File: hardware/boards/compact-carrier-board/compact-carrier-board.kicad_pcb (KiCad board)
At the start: 2 copper layers, 26 x 44 mm, 7 parts

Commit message: fix(pcb): widen 5V net to spec, reposition board, fix stale metadata
5V net was mostly routed at KiCad's 0.6mm default instead of the board's
own documented IPC-2221 target (2A, 1oz copper, 10C rise -> ~0.78mm min).
Widened to 1.0mm for 74.9mm of its 83.9mm total length. The remaining
9mm stays at 0.6mm in two short, unavoidable pinch points (4mm, 5mm)
where the trace passes within 1.27-1.34mm of unrelated J_ESP2 pads and
can't widen without violating clearance. Both pinch points sit downstream
of the branch point that already routes the highest-current load
(J_SERVO) on its own independent, unpinched trace, so worst-case current
through either pinch is bounded by the ESP32 module + J_I2S amp combined
(~1.0-1.1A by datasheet figures, against the pinch's own ~1.65A/10C
capacity) -- real margin, not a bare pass. Verified against Espressif's
ESP32-C3 datasheet (350mA peak WiFi TX) and Analog Devices' MAX98357A
datasheet (3.2W/4ohm rated output, ~700mA computed supply draw at 92%
efficiency).

Widening the traces required refilling the GND copper pour, which
surfaced a real bug: the zone's saved fill went stale relative to the
new geometry, leaving it ~0.0005-0.0015mm from the widened traces --
effectively fused copper, invisible to `kicad-cli pcb drc --refill-zones`
since that flag only recomputes the fill in-memory for the check and
never persists it to the file. A naive Gerber export would have carried
the stale, shorted fill straight into a fab package. Fixed by using
KiCad's own Python API (pcbnew.ZONE_FILLER + pcbnew.SaveBoard) to force
a real refill and re-save; re-verified with `kicad-cli pcb drc` run
*without* --refill-zones specifically to confirm the fix persisted to
disk rather than just passing the same in-memory check again.

Also: repositioned the whole board off the KiCad page origin (was
overlapping the A4 sheet's own border/reference-grid decoration --
cosmetic, no fab effect, verified as an exact rigid translation of every
object); stripped a stale `c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
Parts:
- J_ESP1: footprint carrier:J_ESP1 -> J_ESP1
- J_ESP2: footprint carrier:J_ESP2 -> J_ESP2
- J_I2C_OLED: footprint carrier:J_I2C_OLED -> J_I2C_OLED
- J_I2C_PCA: footprint carrier:J_I2C_PCA -> J_I2C_PCA
- J_I2S: footprint carrier:J_I2S -> J_I2S
- J_PWR: footprint carrier:J_PWR -> J_PWR
- J_SERVO: footprint carrier:J_SERVO -> J_SERVO
- moved J_ESP1 17.7 mm to (25.5, 14.2)
- moved J_ESP2 17.7 mm to (25.5, 29.4)
- moved J_I2C_OLED 17.7 mm to (20.4, 36.5)
- moved J_I2C_PCA 17.7 mm to (20.4, 42.5)
- moved J_I2S 17.7 mm to (31.9, 36.5)
- moved J_PWR 17.7 mm to (21.7, 49.5)
- moved J_SERVO 17.7 mm to (29.3, 49.5)
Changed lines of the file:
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@@
 		)
 	)
-	(footprint "carrier:J_ESP1"
-		(layer "F.Cu")
-		(at 13 1.65)
+	(footprint "J_ESP1"
+		(layer "F.Cu")
+		(at 25.5 14.15)
 		(property "Reference" "J_ESP1"
-			(at -10.466666 -1 0)
+			(at -7.62 2.2 0)
 			(layer "F.SilkS")
 			(effects
@@
 		(embedded_fonts no)
 	)
-	(footprint "carrier:J_I2C_PCA"
-		(layer "F.Cu")
-		(at 7.92 30)
+	(footprint "J_I2C_PCA"
+		(layer "F.Cu")
+		(at 20.42 42.5)
 		(property "Reference" "J_I2C_PCA"
 			(at -4.491429 -2 0)
@@
 		(embedded_fonts no)
 	)
-	(footprint "carrier:J_I2C_OLED"
-		(layer "F.Cu")
-		(at 7.92 24)
+	(footprint "J_I2C_OLED"
+		(layer "F.Cu")
+		(at 20.42 36.5)
 		(property "Reference" "J_I2C_OLED"
 			(at -4.129524 -2 0)
@@
 		(embedded_fonts no)
 	)
-	(footprint "carrier:J_PWR"
-		(layer "F.Cu")
-		(at 9.19 37)
+	(footprint "J_PWR"
+		(layer "F.Cu")
+		(at 21.69 49.5)
 		(property "Reference" "J_PWR"
 			(at -5.01 -2 0)
@@
 		(embedded_fonts no)
 	)
-	(footprint "carrier:J_I2S"
-		(layer "F.Cu")
-		(at 19.35 24)
+	(footprint "J_I2S"
+		(layer "F.Cu")
+		(at 31.85 36.5)
 		(property "Reference" "J_I2S"
 			(at -6.28 -2 0)
@@
 		(embedded_fonts no)
 	)
-	(footprint "carrier:J_ESP2"
-		(layer "F.Cu")
-		(at 13 16.89)
+	(footprint "J_ESP2"
+		(layer "F.Cu")
+		(at 25.5 29.39)
 		(property "Reference" "J_ESP2"
 			(at -10.466666 2.2 0)
@@
 		(embedded_fonts no)
 	)
-	(footprint "carrier:J_SERVO"
-		(layer "F.Cu")
-		(at 16.81 37)
+	(footprint "J_SERVO"
+		(layer "F.Cu")
+		(at 29.31 49.5)
 		(property "Reference" "J_SERVO"
 			(at -2.47 -2 0)
@@
 	)
 	(gr_rect
-		(start 0 0)
-		(end 26 44)
+		(start 12.5 12.5)
+		(end 38.5 56.5)
 		(stroke
 			(width 0.1)
@@
 	)
 	(segment
-		(start 13 37)
-		(end 15.54 37)
-		(width 1)
-		(layer "F.Cu")
-		(net "5V")
-	)
-	(segment
-		(start 2.84 1.65)
-		(end 1.5 10)
+		(start 25.5 49.5)
+		(end 28.04 49.5)
+		(width 1)
+		(layer "F.Cu")
+		(net "5V")
+	)
+	(segment
+		(start 26.77 31.5)
+		(end 26.77 36.5)
+		(width 1)
+		(layer "B.Cu")
+		(net "5V")
+	)
+	(segment
+		(start 15.34 14.15)
+		(end 14 22.5)
+		(width 1)
+		(layer "B.Cu")
+		(net "5V")
+	)
+	(segment
+		(start 14 27)
+		(end 14 32)
 		(width 0.6)
 		(layer "B.Cu")
@@
 	)
 	(segment
-		(start 1 12)
-		(end 14.27 14)
+		(start 13.5 24.5)
+		(end 26.77 26.5)
+		(width 1)
+		(layer "B.Cu")
+		(net "5V")
+	)
+	(segment
+		(start 26.77 26.5)
+		(end 26.77 27.5)
+		(width 1)
+		(layer "B.Cu")
+		(net "5V")
+	)
+	(segment
+		(start 13.5 16.5)
+		(end 13.5 24.5)
+		(width 1)
+		(layer "B.Cu")
+		(net "5V")
+	)
+	(segment
+		(start 15.34 14.15)
+		(end 13.5 16.5)
+		(width 1)
+		(layer "B.Cu")
+		(net "5V")
+	)
+	(segment
+		(start 14 46.5)
+		(end 25.5 46.5)
+		(width 1)
+		(layer "B.Cu")
+		(net "5V")
+	)
+	(segment
+		(start 14 22.5)
+		(end 14 27)
+		(width 1)
+		(layer "B.Cu")
+		(net "5V")
+	)
+	(segment
+		(start 14 32)
+		(end 14 46.5)
+		(width 1)
+		(layer "B.Cu")
+		(net "5V")
+	)
+	(segment
+		(start 26.77 27.5)
+		(end 26.77 31.5)
 		(width 0.6)
 		(layer "B.Cu")
@@
 	)
 	(segment
-		(start 14.27 14)
-		(end 14.27 24)
-		(width 0.6)
-		(layer "B.Cu")
-		(net "5V")
-	)
-	(segment
-		(start 1 4)
-		(end 1 12)
-		(width 0.6)
-		(layer "B.Cu")
-		(net "5V")
-	)
-	(segment
-		(start 2.84 1.65)
-		(end 1 4)
-		(width 0.6)
-		(layer "B.Cu")
-		(net "5V")
-	)
-	(segment
-		(start 1.5 34)
-		(end 13 34)
-		(width 0.6)
-		(layer "B.Cu")
-		(net "5V")
-	)
-	(segment
-		(start 1.5 10)
-		(end 1.5 34)
-		(width 0.6)
-		(layer "B.Cu")
-		(net "5V")
-	)
-	(segment
-		(start 13 34)
-		(end 13 37)
-		(width 0.6)
-		(layer "B.Cu")
-		(net "5V")
-	)
-	(segment
-		(start 11.73 24)
-		(end 11.73 30)
+		(start 25.5 46.5)
+		(end 25.5 49.5)
+		(width 1)
+		(layer "B.Cu")
+		(net "5V")
+	)
+	(segment
+		(start 24.23 36.5)
+		(end 24.23 42.5)
 		(width 0.3)
 		(layer "F.Cu")
@@
 	)
 	(segment
-		(start 4.11 24)
-		(end 4.11 30)
+		(start 16.61 36.5)
+		(end 16.61 42.5)
 		(width 0.25)
 		(layer "F.Cu")
@@
 	)
 	(segment
-		(start 7.92 1.65)
-		(end 4.11 16.89)
+		(start 20.42 14.15)
+		(end 16.61 29.39)
 		(width 0.3)
 		(layer "F.Cu")
@@
 	)
 	(segment
-		(start 4.11 16.89)
-		(end 4.11 24)
+		(start 16.61 29.39)
+		(end 16.61 36.5)
 		(width 0.3)
 		(layer "F.Cu")
@@
 	)
 	(segment
-		(start 10.46 1.65)
-		(end 6.65 16.89)
+		(start 22.96 14.15)
+		(end 19.15 29.39)
 		(width 0.25)
 		(layer "F.Cu")
@@
 	)
 	(segment
-		(start 6.65 24)
-		(end 6.65 30)
+		(start 19.15 36.5)
+		(end 19.15 42.5)
 		(width 0.25)
 		(layer "F.Cu")
@@
 	)
 	(segment
-		(start 6.65 16.89)
-		(end 6.65 24)
+		(start 19.15 29.39)
+		(end 19.15 36.5)
 		(width 0.25)
 		(layer "F.Cu")
@@
 	)
 	(segment
-		(start 9.19 24)
-		(end 9.19 30)
+		(start 21.69 36.5)
+		(end 21.69 42.5)
 		(width 0.25)
 		(layer "F.Cu")
@@
 	)
 	(segment
-		(start 13 1.65)
-		(end 9.19 16.89)
+		(start 25.5 14.15)
+		(end 21.69 29.39)
 		(width 0.25)
 		(layer "F.Cu")
@@
 	)
 	(segment
-		(start 9.19 16.89)
-		(end 9.19 24)
+		(start 21.69 29.39)
+		(end 21.69 36.5)
 		(width 0.25)
 		(layer "F.Cu")
@@
 	)
 	(segment
-		(start 15.54 1.65)
-		(end 16.81 16.89)
+		(start 28.04 14.15)
+		(end 29.31 29.39)
 		(width 0.25)
 		(layer "B.Cu")
@@
 	)
 	(segment
-		(start 16.81 16.89)
-		(end 16.81 24)
+		(start 29.31 29.39)
+		(end 29.31 36.5)
 		(width 0.25)
 		(layer "B.Cu")
@@
 	)
 	(segment
-		(start 18.08 1.65)
-		(end 19.35 16.89)
+		(start 30.58 14.15)
+		(end 31.85 29.39)
 		(width 0.25)
 		(layer "B.Cu")
@@
 	)
 	(segment
-		(start 19.35 16.89)
-		(end 19.35 24)
+		(start 31.85 29.39)
+		(end 31.85 36.5)
 		(width 0.25)
 		(layer "B.Cu")
@@
 	)
 	(segment
-		(start 21.89 16.89)
-		(end 21.89 24)
+		(start 34.39 29.39)
+		(end 34.39 36.5)
 		(width 0.25)
 		(layer "B.Cu")
@@
 	)
 	(segment
-		(start 20.62 1.65)
-		(end 21.89 16.89)
+		(start 33.12 14.15)
+		(end 34.39 29.39)
 		(width 0.25)
 		(layer "B.Cu")
@@
 	)
 	(segment
-		(start 7.92 16.89)
-		(end 7.92 37)
+		(start 20.42 29.39)
+		(end 20.42 49.5)
 		(width 0.3)
 		(layer "F.Cu")
@@
 	)
 	(segment
-		(start 10.46 16.89)
-		(end 10.46 37)
+		(start 22.96 29.39)
+		(end 22.96 49.5)
 		(width 0.3)
 		(layer "F.Cu")
@@
 		(polygon
 			(pts
-				(xy 0.5 0.5) (xy 25.5 0.5) (xy 25.5 43.5) (xy 0.5 43.5)
-			)
-		)
+				(xy 13 13) (xy 38 13) (xy 38 56) (xy 13 56)
+			)
+		)

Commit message: carrier-board: fix mirrored ESP socket, add pin-name silkscreen
The two 1x9 socket rows carried each other's nets: the pad map was the
C3-Zero seen from its PIN side, which is only correct for a socket on the
opposite face. As drawn, a component-side-up module could not mate — 5V
would have landed on GP5.

Caught by handedness, which no rotation can change: on the module
(component side, USB-C up) pins 1-9 run down the left column and 10-18 up
the right, so 1->18 is counter-clockwise; on the old artwork J_ESP1 1->9 ran
left-to-right along the outer row and J_ESP2 10->18 right-to-left along the
inner row, i.e. clockwise.

Swap the two footprints' Y positions (14.15 <-> 29.39) so the nets land on
the correct rows, and re-route. Nothing mechanical moves: the exported
PTH.drl and Edge_Cuts.gm1 are byte-identical to the previous revision, all
37 holes stay at 0.9mm, and the five wire-end connectors do not move. The
module's USB-C still overhangs the 5V-bus edge.

Re-route side effects, all measured:
- 5V: 83.901mm with 9mm at 0.600mm -> 44.939mm entirely at 1.000mm, so the
  net now meets its own IPC-2221 target everywhere; an acute-angle acid
  trap at the old 5V pad is gone.
- 3V3/SDA/SCL moved to B.Cu (all pads are THT, so no vias), which frees
  F.Cu for D+/D- to pass the row they now cross.
- D+/D-: 20.110 -> 36.088mm each, exactly length-matched, one 1.27mm jog
  per line at 0.420mm to the nearest pad edge (was 0.270mm worst case).
- GND pour +6.9%, one island, all six GND pads on 4 thermal spokes.

Add the silkscreen that would have made this visible: 18 socket pin names
and a USB-end arrow at 1.0mm/0.15mm, JLCPCB's standard-font minimum. The
board previously carried nothing but seven reference designators. Placement
was verified geometrically, not by DRC — this project sets
min_silk_clearance to 0, so DRC would not flag an overlap.

kicad-cli pcb drc --severity-all, run without --refill-zones: 0 violations,
0 unconnected items. The on-disk zone fill is vertex-exa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
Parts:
- moved J_ESP1 15.2 mm to (25.5, 29.4)
- moved J_ESP2 15.2 mm to (25.5, 14.2)
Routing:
- net 5V: track 83.9 -> 44.9 mm
- net USB_DP: track 20.1 -> 36.1 mm
- net USB_DM: track 20.1 -> 36.1 mm
- net BCLK: track 22.4 -> 7.33 mm
- net LRCLK: track 22.4 -> 7.33 mm
- net DIN: track 22.4 -> 7.33 mm
- net SCL: track 28.8 -> 14.7 mm
- net SDA: track 28.8 -> 14.7 mm
- net 3V3: track 28.8 -> 14.7 mm
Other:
- board text added: "3V3"
- board text added: "5V"
- board text added: "GND"
- board text added: "GP0"
- board text added: "GP1"
- board text added: "GP10"
- board text added: "GP18"
- board text added: "GP19"
- board text added: "GP2"
- board text added: "GP20"
- board text added: "GP21"
- board text added: "GP3"
- board text added: "GP4"
- board text added: "GP5"
- board text added: "GP6"
- board text added: "GP7"
- board text added: "GP8"
- board text added: "GP9"
- board text added: "USB"

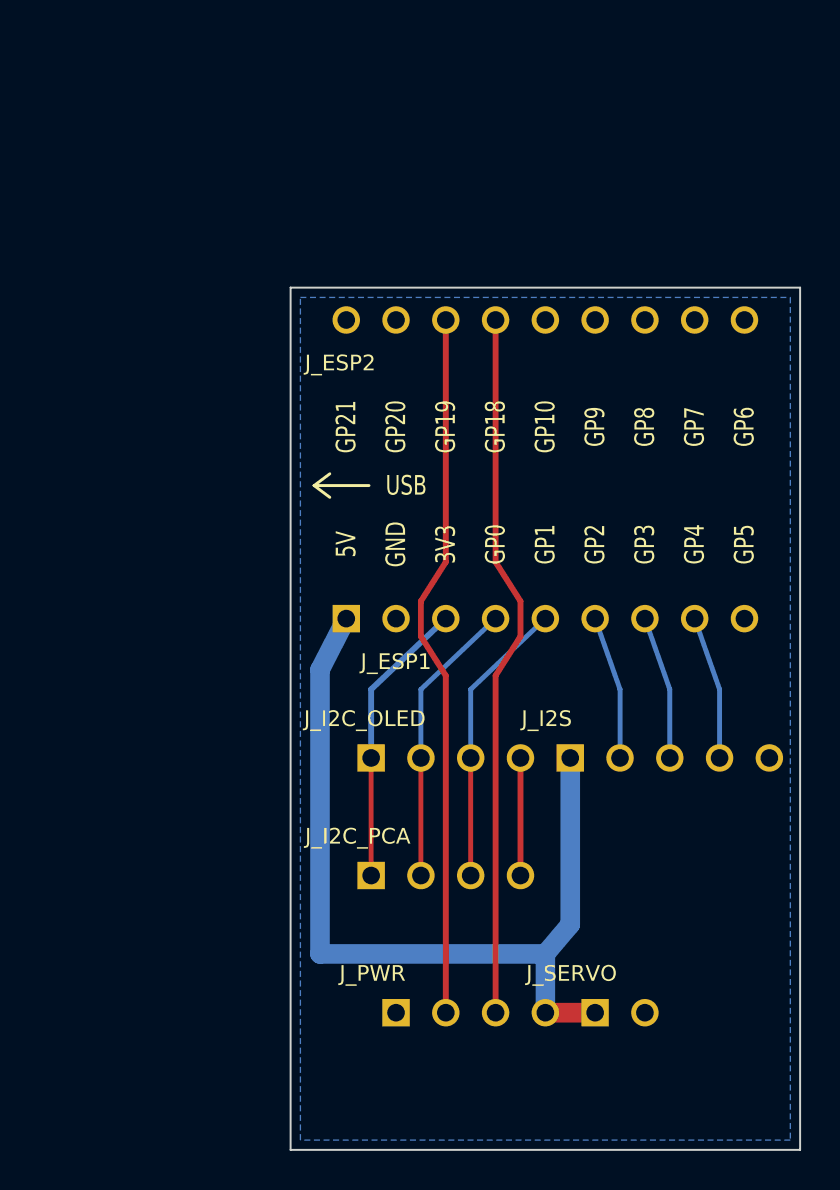
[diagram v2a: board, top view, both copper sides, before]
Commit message: carrier-board: name every pad on silk, raise the clearance floors
Three loose ends from the row-swap revision.

Pin names for the wire-end connectors. Every pad on the board is now
labelled: 3V3/SDA/SCL/GND on both I2C headers, 5V/BCLK/LRC/DIN/GND on
J_I2S, GND/D+/D-/5V on J_PWR, 5V/GND on J_SERVO, alongside the socket rows
and the USB arrow added in the previous commit. J_I2C_PCA, J_PWR and
J_SERVO designators moved to clear the new label bands. 48 silk items in
total.

Reference designators to JLCPCB's standard font. They were 0.8mm high with
a 0.12mm stroke, below the 1.0mm/0.15mm standard-font minimum and passing
DRC only because min_text_thickness was 0.08. All seven are now 1.0/0.15,
with each label re-checked against the 0.30mm edge margin - three sit at
exactly that margin, so the larger boxes were nudged back inside instead of
being allowed to overhang.

GND pour clearance 0.20 -> 0.25mm (the zone's local clearance and the
Default netclass together), then refilled. At 0.20 the fill sat at exactly
JLCPCB's floor with nothing left for their etch tolerance; the nearest
track-based constraint is 0.42mm, so the extra 0.05mm costs no geometry.

Raise the DRC floors so a passing run means something: min_clearance
0.0 -> 0.2, min_silk_clearance 0.0 -> 0.15, min_text_height 0.8 -> 1.0,
min_text_thickness 0.08 -> 0.15. At the old settings DRC could not fail on
clearance, silk overlap or undersized text however bad they got - which is
part of why the mirrored pad map and the 0.6mm 5V sections both survived
review.

Silk placement is still verified geometrically rather than trusted to DRC:
0 silk-to-silk overlaps, 0.421mm minimum silk-to-pad, 0.383mm minimum
silk-to-edge. kicad-cli pcb drc --severity-all under the new floors, run
without --refill-zones: 0 violations, 0 unconnected items. Render
regenerated.

Co-Authored-By: Claude Opus 5 <noreply@anthropic.com>
Claude-Session: https://claude.ai/code/session_01GboNwm1xyFSrjmjdTVYzzi
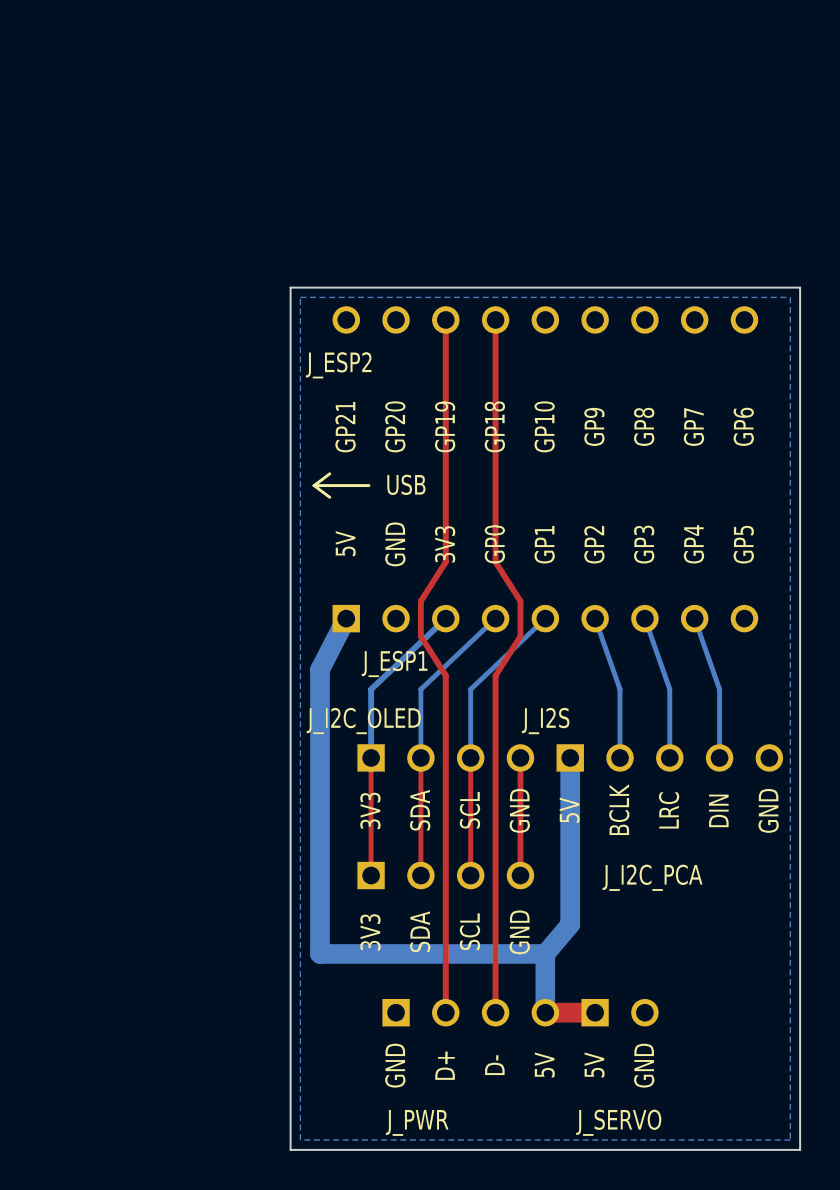
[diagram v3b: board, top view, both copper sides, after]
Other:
- board text added: "BCLK"
- board text added: "D+"
- board text added: "D-"
- board text added: "DIN"
- board text added: "LRC"
- board text added: "SCL"
- board text added: "SDA"
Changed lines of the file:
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@@
 			(effects
 				(font
-					(size 0.8 0.8)
-					(thickness 0.12)
+					(size 1 0.75)
+					(thickness 0.15)
 				)
 			)
@@
 		(at 20.42 42.5)
 		(property "Reference" "J_I2C_PCA"
-			(at -4.491429 -2 0)
+			(at 10.58 0 0)
 			(layer "F.SilkS")
 			(effects
 				(font
-					(size 0.8 0.8)
-					(thickness 0.12)
+					(size 1 0.75)
+					(thickness 0.15)
 				)
 			)
@@
 			(effects
 				(font
-					(size 0.8 0.8)
-					(thickness 0.12)
+					(size 1 0.75)
+					(thickness 0.15)
 				)
 			)
@@
 		(at 21.69 49.5)
 		(property "Reference" "J_PWR"
-			(at -5.01 -2 0)
+			(at -2.69 5.5 0)
 			(layer "F.SilkS")
 			(effects
 				(font
-					(size 0.8 0.8)
-					(thickness 0.12)
+					(size 1 0.75)
+					(thickness 0.15)
 				)
 			)
@@
 			(effects
 				(font
-					(size 0.8 0.8)
-					(thickness 0.12)
+					(size 1 0.75)
+					(thickness 0.15)
 				)
 			)
@@
 			(effects
 				(font
-					(size 0.8 0.8)
-					(thickness 0.12)
+					(size 1 0.75)
+					(thickness 0.15)
 				)
 			)
@@
 		(at 29.31 49.5)
 		(property "Reference" "J_SERVO"
-			(at -2.47 -2 0)
+			(at -0.01 5.5 0)
 			(layer "F.SilkS")
 			(effects
 				(font
-					(size 0.8 0.8)
-					(thickness 0.12)
+					(size 1 0.75)
+					(thickness 0.15)
 				)
 			)
@@
 		)
 	)
+	(gr_text "3V3"
+		(at 16.61 39.2 90)
+		(layer "F.SilkS")
+		(effects
+			(font
+				(size 1 0.75)
+				(thickness 0.15)
+			)
+		)
+	)
+	(gr_text "3V3"
+		(at 16.61 45.4 90)
+		(layer "F.SilkS")
+		(effects
+			(font
+				(size 1 0.75)
+				(thickness 0.15)
+			)
+		)
+	)
 	(gr_text "GP20"
 		(at 17.88 19.6 90)
@@
 		)
 	)
+	(gr_text "GND"
+		(at 17.88 52.2 90)
+		(layer "F.SilkS")
+		(effects
+			(font
+				(size 1 0.75)
+				(thickness 0.15)
+			)
+		)
+	)
+	(gr_text "SDA"
+		(at 19.15 39.2 90)
+		(layer "F.SilkS")
+		(effects
+			(font
+				(size 1 0.75)
+				(thickness 0.15)
+			)
+		)
+	)
+	(gr_text "SDA"
+		(at 19.15 45.4 90)
+		(layer "F.SilkS")
+		(effects
+			(font
+				(size 1 0.75)
+				(thickness 0.15)
+			)
+		)
+	)
 	(gr_text "GP19"
 		(at 20.42 19.6 90)
@@
 		)
 	)
+	(gr_text "D+"
+		(at 20.42 52.2 90)
+		(layer "F.SilkS")
+		(effects
+			(font
+				(size 1 0.75)
+				(thickness 0.15)
+			)
+		)
+	)
+	(gr_text "SCL"
+		(at 21.69 39.2 90)
+		(layer "F.SilkS")
+		(effects
+			(font
+				(size 1 0.75)
+				(thickness 0.15)
+			)
+		)
+	)
+	(gr_text "SCL"
+		(at 21.69 45.4 90)
+		(layer "F.SilkS")
+		(effects
+			(font
+				(size 1 0.75)
+				(thickness 0.15)
+			)
+		)
+	)
 	(gr_text "GP18"
 		(at 22.96 19.6 90)
@@
 		)
 	)
+	(gr_text "D-"
+		(at 22.96 52.2 90)
+		(layer "F.SilkS")
+		(effects
+			(font
+				(size 1 0.75)
+				(thickness 0.15)
+			)
+		)
+	)
+	(gr_text "GND"
+		(at 24.23 39.2 90)
+		(layer "F.SilkS")
+		(effects
+			(font
+				(size 1 0.75)
+				(thickness 0.15)
+			)
+		)
+	)
+	(gr_text "GND"
+		(at 24.23 45.4 90)
+		(layer "F.SilkS")
+		(effects
+			(font
+				(size 1 0.75)
+				(thickness 0.15)
+			)
+		)
+	)
 	(gr_text "GP10"
 		(at 25.5 19.6 90)
@@
 		)
 	)
+	(gr_text "5V"
+		(at 25.5 52.2 90)
+		(layer "F.SilkS")
+		(effects
+			(font
+				(size 1 0.75)
+				(thickness 0.15)
+			)
+		)
+	)
+	(gr_text "5V"
+		(at 26.77 39.2 90)
+		(layer "F.SilkS")
+		(effects
+			(font
+				(size 1 0.75)
+				(thickness 0.15)
+			)
+		)
+	)
 	(gr_text "GP9"
 		(at 28.04 19.6 90)
@@
 		)
 	)
+	(gr_text "5V"
+		(at 28.04 52.2 90)
+		(layer "F.SilkS")
+		(effects
+			(font
+				(size 1 0.75)
+				(thickness 0.15)
+			)
+		)
+	)
+	(gr_text "BCLK"
+		(at 29.31 39.2 90)
+		(layer "F.SilkS")
+		(effects
+			(font
+				(size 1 0.75)
+				(thickness 0.15)
+			)
+		)
+	)
 	(gr_text "GP8"
 		(at 30.58 19.6 90)
@@
 		)
 	)
+	(gr_text "GND"
+		(at 30.58 52.2 90)
+		(layer "F.SilkS")
+		(effects
+			(font
+				(size 1 0.75)
+				(thickness 0.15)
+			)
+		)
+	)
+	(gr_text "LRC"
+		(at 31.85 39.2 90)
+		(layer "F.SilkS")
+		(effects
+			(font
+				(size 1 0.75)
+				(thickness 0.15)
+			)
+		)
+	)
 	(gr_text "GP7"
 		(at 33.119999 19.6 90)
@@
 		)
 	)
+	(gr_text "DIN"
+		(at 34.39 39.2 90)
+		(layer "F.SilkS")
+		(effects
+			(font
+				(size 1 0.75)
+				(thickness 0.15)
+			)
+		)
+	)
 	(gr_text "GP6"
 		(at 35.66 19.6 90)
@@
 	(gr_text "GP5"
 		(at 35.66 25.6 90)
+		(layer "F.SilkS")
+		(effects
+			(font
+				(size 1 0.75)
+				(thickness 0.15)
+			)
+		)
+	)
+	(gr_text "GND"
+		(at 36.93 39.2 90)
 		(layer "F.SilkS")
 		(effects
@@
 		(hatch edge 0.5)
 		(connect_pads
-			(clearance 0.2)
+			(clearance 0.25)
 		)
 		(min_thickness 0.15)
